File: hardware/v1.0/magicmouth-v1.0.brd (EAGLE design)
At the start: 68.6 x 53.3 mm, 110 parts, among them IC1 LM386N, IC2 ATMEGA328P_PDIP, Q1 16Mhz, U1 ARDUINOR3-NOIOREF-NOTEXT

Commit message: firmware initial commit
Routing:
- net N$22: track 29.1 -> 13.2 mm
- net N$21: track 26.5 -> 15.3 mm
- net N$20: track 35.3 -> 25.9 mm
- net +5V: track 86.4 -> 79.5 mm
- net N$19: track 29.4 -> 26.3 mm
- net GND: vias 19 -> 24

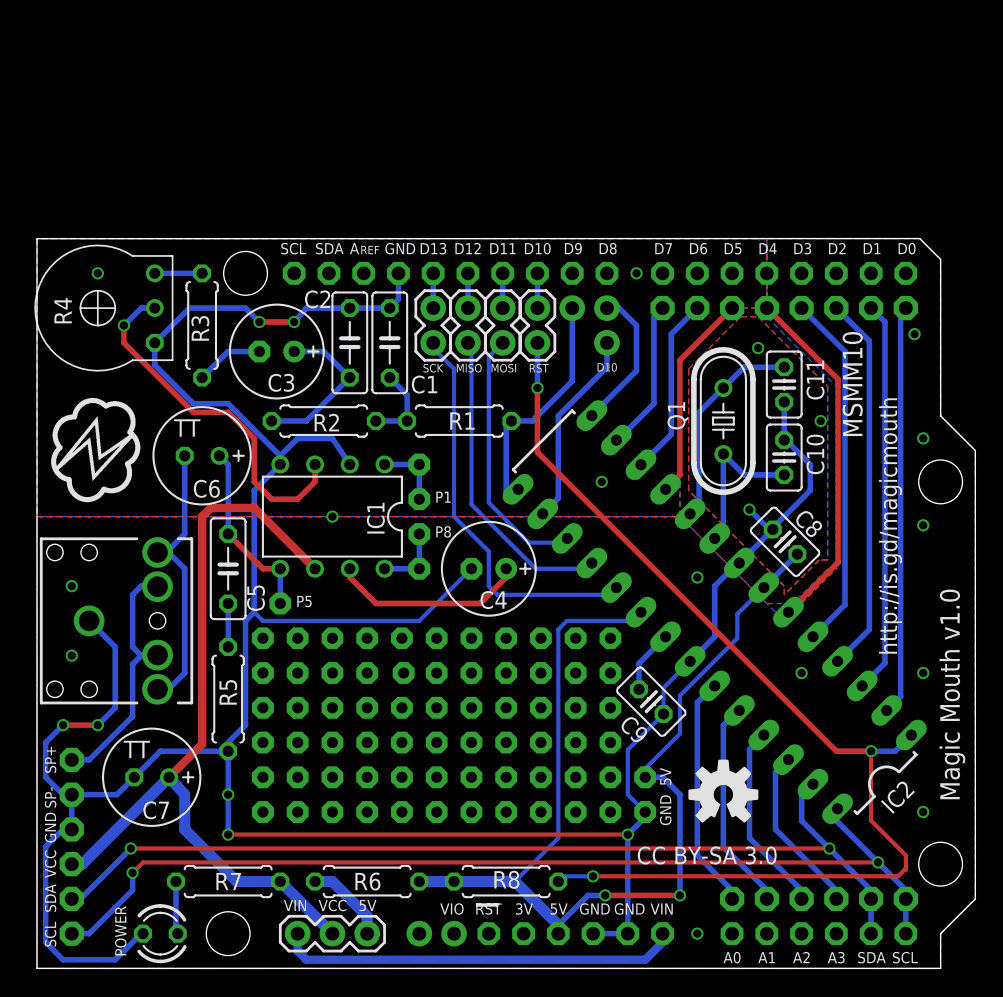
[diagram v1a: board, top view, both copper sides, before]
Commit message: pullup resistors on SDA and SCL
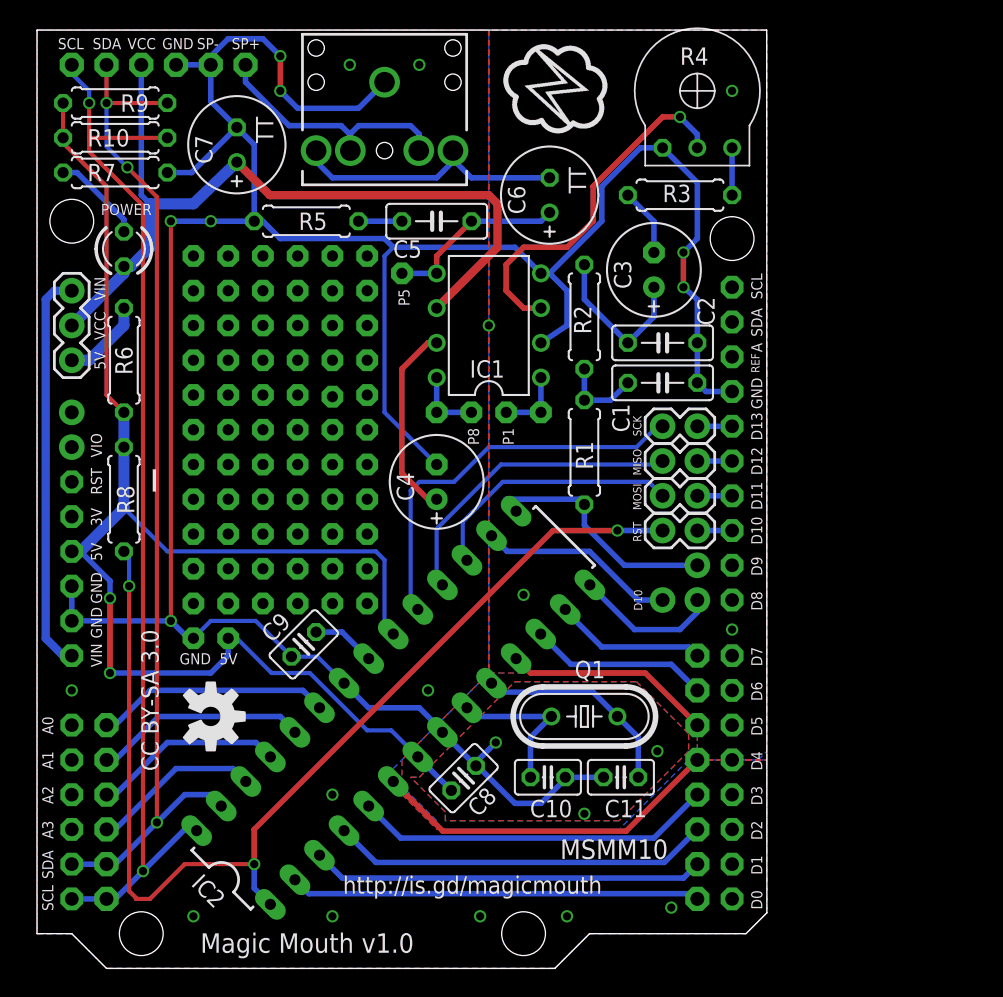
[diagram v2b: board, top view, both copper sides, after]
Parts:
- added R10, R9: 4K7, rcl:0207/7
- moved U1 68.6 mm to (0.00, 68.6), turned to 270 degrees
- moved JP3 57.5 mm to (8.89, 66.0), turned to 180 degrees
- moved R7 52.5 mm to (5.71, 58.2)
- moved JP4 52.5 mm to (5.08, 11.4), turned to 270 degrees
- moved POWER 50.1 mm to (6.35, 52.6), turned to 90 degrees
- moved JP1 47.1 mm to (2.54, 44.5), turned to 90 degrees
- moved C7 46.6 mm to (14.6, 60.2), turned to 90 degrees
- moved R4 46.6 mm to (48.3, 64.1), turned to 0 degrees
- moved JP12 45.8 mm to (2.54, 40.6), turned to 270 degrees
- moved JP2 44.9 mm to (25.4, 64.8), turned to 270 degrees
- moved R6 42.0 mm to (6.35, 44.5), turned to 270 degrees
- moved PAD7 41.0 mm to (11.4, 52.1), turned to 270 degrees
- moved R8 39.5 mm to (6.35, 34.3), turned to 90 degrees
- moved PAD8 38.9 mm to (11.4, 49.5), turned to 270 degrees
- moved PAD40 38.2 mm to (14.0, 52.1), turned to 0 degrees
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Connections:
- net +5V: now also R10.1, R9.1
- net GND: now also R7.2; no longer POWER.K
- net N$10: now also POWER.K; no longer POWER.A
- net SCL: now also R10.2
- net SDA: now also R9.2
- net VCC: now also POWER.A; no longer R7.2
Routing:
- net +5V: track 79.5 -> 104.0 mm
- net GND: track 220.7 -> 209.3 mm
- net SCL: track 73.2 -> 78.2 mm
- net SDA: track 70.3 -> 74.8 mm, vias 2 -> 3
- net N$10: track 3.86 -> 6.75 mm
- net VCC: track 58.4 -> 59.5 mm
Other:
- board size 68.6 x 53.3 mm -> 53.3 x 68.6 mm

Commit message: adjusted position of trimpot, enlarged small text
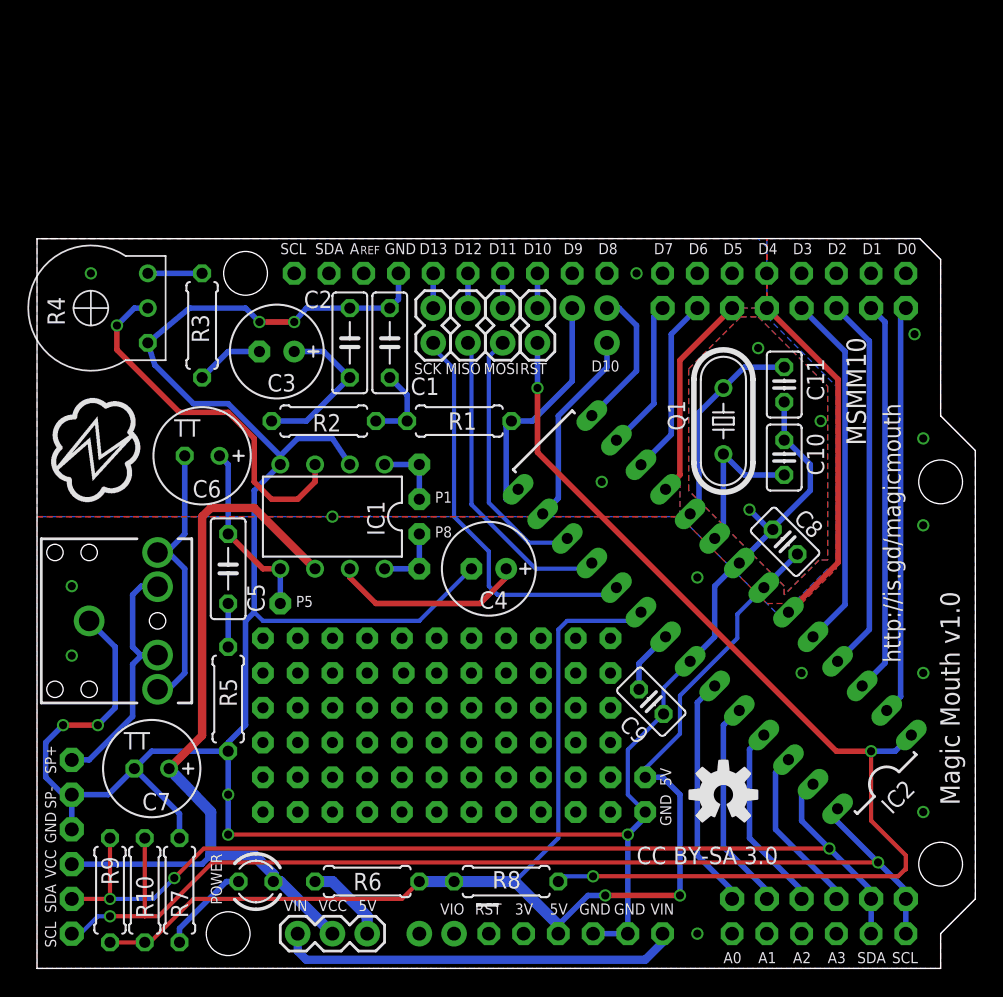
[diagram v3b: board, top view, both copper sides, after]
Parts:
- moved U1 68.6 mm to (0.00, 0.00), turned to 0 degrees
- moved R9 57.5 mm to (5.33, 5.71), turned to 90 degrees
- moved JP3 57.5 mm to (2.54, 8.89), turned to 270 degrees
- moved R10 55.0 mm to (7.87, 5.71), turned to 90 degrees
- moved R7 52.7 mm to (10.4, 5.71), turned to 90 degrees
- moved JP4 52.5 mm to (57.1, 5.08), turned to 0 degrees
- moved POWER 47.2 mm to (16.0, 6.35), turned to 180 degrees
- moved JP1 47.1 mm to (24.1, 2.54), turned to 180 degrees
- moved R4 47.1 mm to (3.94, 48.3), turned to 90 degrees
- moved C7 46.0 mm to (8.38, 14.6), turned to 180 degrees
- moved JP12 45.8 mm to (27.9, 2.54), turned to 0 degrees
- moved JP2 44.9 mm to (3.81, 25.4), turned to 0 degrees
- moved R6 42.0 mm to (24.1, 6.35), turned to 0 degrees
- moved PAD7 41.0 mm to (16.5, 11.4), turned to 0 degrees
- moved R8 39.5 mm to (34.3, 6.35), turned to 180 degrees
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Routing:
- net N$9: track 26.4 -> 27.2 mm
- net N$5: track 3.46 -> 3.97 mm
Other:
- board size 53.3 x 68.6 mm -> 68.6 x 53.3 mm

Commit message: copied magic smoke logo on bottom
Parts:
- added U$2: (no value), SparkFun:OSHW-LOGO-M
